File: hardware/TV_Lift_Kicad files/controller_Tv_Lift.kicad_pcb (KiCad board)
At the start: 4 copper layers, 70 x 157.5 mm, 102 parts, among them J1 socket LAN8720a, J10 1844210, J11 1844223, J12 C5360899, J2 1836189, J3 1844223, J4 1844210, J5 1844223, J6 1844223, J7 1844236, J8 C5360899, J9 1844210, Q2 MMBT3906, SW1 TS-1187A-BAB, SW2 TS-1187A-BAB, SW3 TS-1187A-BAB, SW4 TS-1187A-BAB, U1 MAX3232, U10 VNH5019A-E, U2 TSOP32S40F, U3 SN65HVD230, U4 ESP32-WROOM-32, U5 LM2596S-5, U6 AMS1117-3.3, U7 PC817, U8 PC817, U9 b0505s-1we

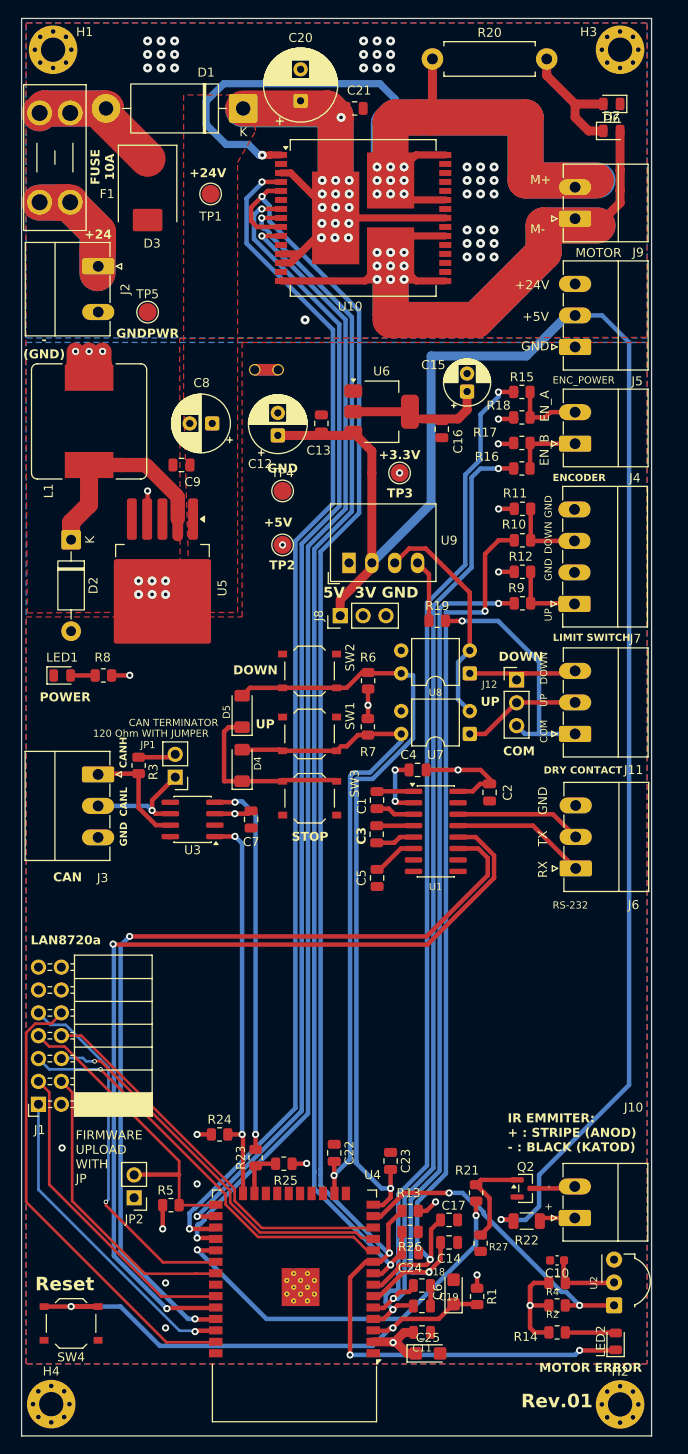
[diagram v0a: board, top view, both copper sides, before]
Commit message: finish pcb board change pins
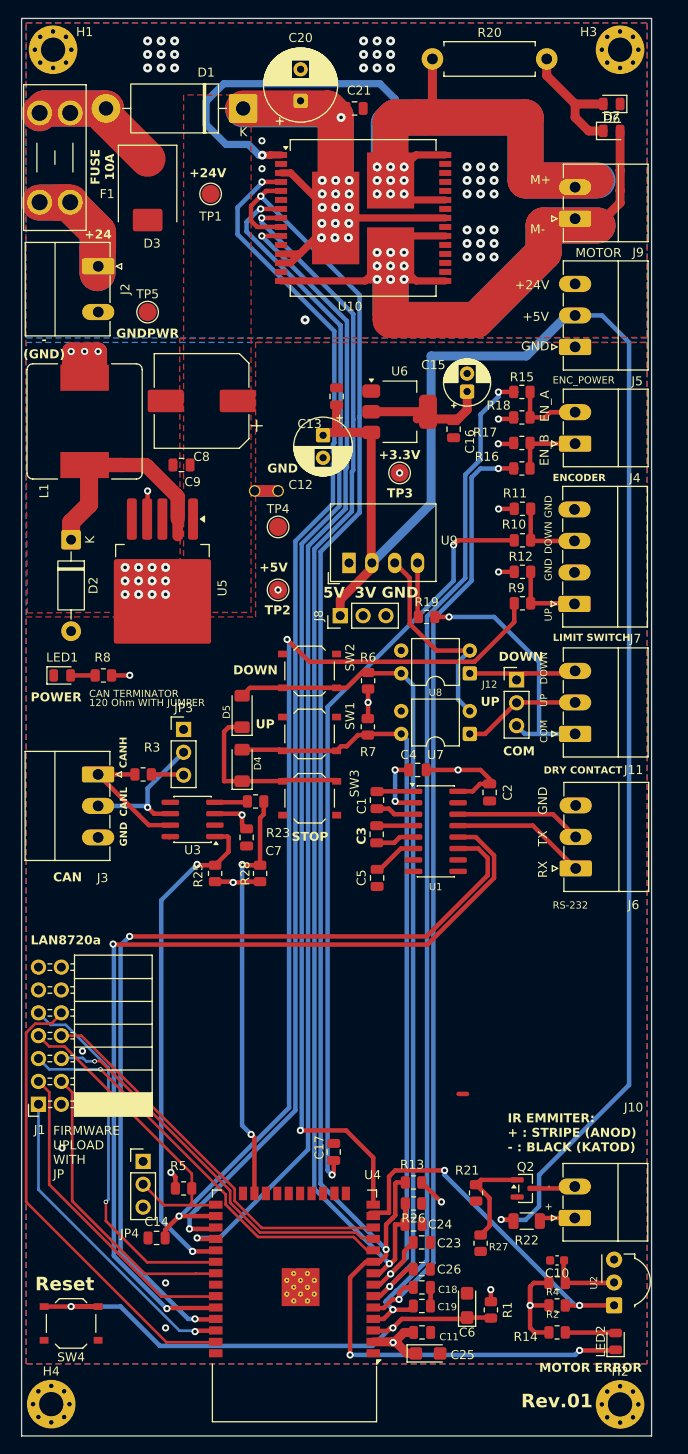
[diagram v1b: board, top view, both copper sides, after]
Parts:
- removed C22: 100 nF 16V, Capacitor_SMD:C_0805_2012Metric
- removed JP1: CAN_Jumper, Connector_PinHeader_2.54mm:PinHeader_1x02_P2.54mm_Vertical
- removed JP2: FIRMWARE_Jumper, Connector_PinHeader_2.54mm:PinHeader_1x02_P2.54mm_Vertical
- removed R24: 10k, Resistor_SMD:R_0805_2012Metric
- added C26: 100 nF 16V, Capacitor_SMD:C_0805_2012Metric, F.Cu at (110.0, 164.5)
- added JP3: C5360899, Connector_PinHeader_2.54mm:PinHeader_1x03_P2.54mm_Vertical, F.Cu at (83.5, 104.5)
- added JP4: C5360899, Connector_PinHeader_2.54mm:PinHeader_1x03_P2.54mm_Vertical, F.Cu at (79.0, 152.5)
- added R28: 10k, Resistor_SMD:R_0805_2012Metric, F.Cu at (92.0, 120.5)
- C12: value 470 uF 16V -> 220 uF 16V
- C8: value 220 uF 50V Low ESR -> C46550473; footprint Capacitor_THT:CP_Radial_D6.3mm_P2.50mm -> Capacitor_SMD:CP_Elec_10x10
- U10: value VNH5019A-E -> VNH5019ATR-E
- moved R23 39.6 mm to (91.5, 112.5), turned to 180 degrees
- moved R25 33.1 mm to (87.0, 120.5), turned to 90 degrees
- moved C14 32.5 mm to (80.5, 161.0), turned to 180 degrees
- moved C17 14.9 mm to (100.2, 151.4), turned to 90 degrees
- moved NT2 13.5 mm to (94.0, 78.0)
- moved C23 9.69 mm to (110.0, 161.5), turned to 0 degrees
- moved C12 5.03 mm to (99.0, 71.8), turned to -90 degrees
- moved TP2 5.02 mm to (94.0, 89.0)
- moved TP4 4.03 mm to (94.0, 82.0)
- moved C13 3.44 mm to (100.5, 67.5)
- moved C24 3.19 mm to (109.0, 159.5)
- moved R13 3.19 mm to (109.0, 154.8)
- moved R26 3.19 mm to (109.0, 157.2)
- moved C8 2.77 mm to (85.5, 68.0)
- moved R5 2.33 mm to (83.5, 155.5)
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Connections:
- C23 pad 1: GND -> /DRY_CONTACT_UP
- C23 pad 2: /DRY_CONTACT_DOWN -> GND
- C7 pad 1: GND -> +3.3V
- C7 pad 2: +3.3V -> GND
- R21 pad 2: /IR_BLASTER -> /IR_TRANSMITTER
- R25 pad 2: /CAN_RX -> /CAN_TX
- R3 pad 1: Net-(JP1-B) -> Net-(J3-Pin_1)
- R3 pad 2: Net-(J3-Pin_1) -> Net-(JP3-B)
- U4 pad 14: /DRY_CONTACT_DOWN -> /M1_PWM
- U4 pad 16: /DRY_CONTACT_UP -> /M1_LIMIT_DOWN
- U4 pad 24: /CAN_TX -> /IR_TRANSMITTER
- U4 pad 26: /M1_PWM -> /M1_LIMIT_UP
- U4 pad 29: /IR_BLASTER -> /CAN_TX
- U4 pad 6: /M1_LIMIT_UP -> /DRY_CONTACT_DOWN
- U4 pad 7: /M1_LIMIT_DOWN -> /DRY_CONTACT_UP
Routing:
- net /IR_BLASTER: track 44.5 -> 0.00 mm, vias 2 -> 0
- net /CAN_RX: track 5.44 -> 46.4 mm, vias 0 -> 2
- net Net-(U3-R): track 42.5 -> 3.65 mm, vias 2 -> 0
- net /M1_LIMIT_DOWN: track 101.4 -> 84.7 mm
- net +5V: track 200.6 -> 213.4 mm
- net /CAN_TX: track 43.9 -> 56.0 mm
- net /DRY_CONTACT_UP: track 75.3 -> 86.5 mm
- net /M1_LIMIT_UP: track 97.0 -> 106.6 mm
- net /DRY_CONTACT_DOWN: track 88.5 -> 94.3 mm
- net /IR_REMOTE: track 34.7 -> 39.5 mm
- net Net-(JP1-B): track 4.20 -> 0.00 mm
- net /M1_CS: track 134.6 -> 138.3 mm
- net Net-(JP3-B): track 0.00 -> 3.62 mm
- net /M1_DIAG: track 185.1 -> 188.4 mm
- net Net-(J3-Pin_2): track 13.1 -> 16.2 mm
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
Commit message: fix run-on log
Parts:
- moved R21 2.92 mm to (117.5, 153.5), turned to 90 degrees
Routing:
- net /IR_TRANSMITTER: track 0.00 -> 36.5 mm
- net Net-(J9-M-): track 168.6 -> 164.6 mm
- net /M1_LIMIT_DOWN: track 84.7 -> 86.8 mm
- net GND: track 4.14 -> 2.13 mm
- net Net-(Q2-B): track 11.4 -> 9.44 mm
- net +5V: track 213.4 -> 211.5 mm
- net Net-(U4-EN): track 61.4 -> 60.7 mm
